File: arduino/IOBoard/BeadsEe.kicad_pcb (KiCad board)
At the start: 2 copper layers, 68.6 x 53.3 mm, 121 parts, among them J1 Servo Conn, J2 Servo Pow, J3 Supply Select, J4 I2C, P1 Power, P2 Analog, P3 Digital, P4 Digital, P5 CONN_01X01, P6 CONN_01X01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

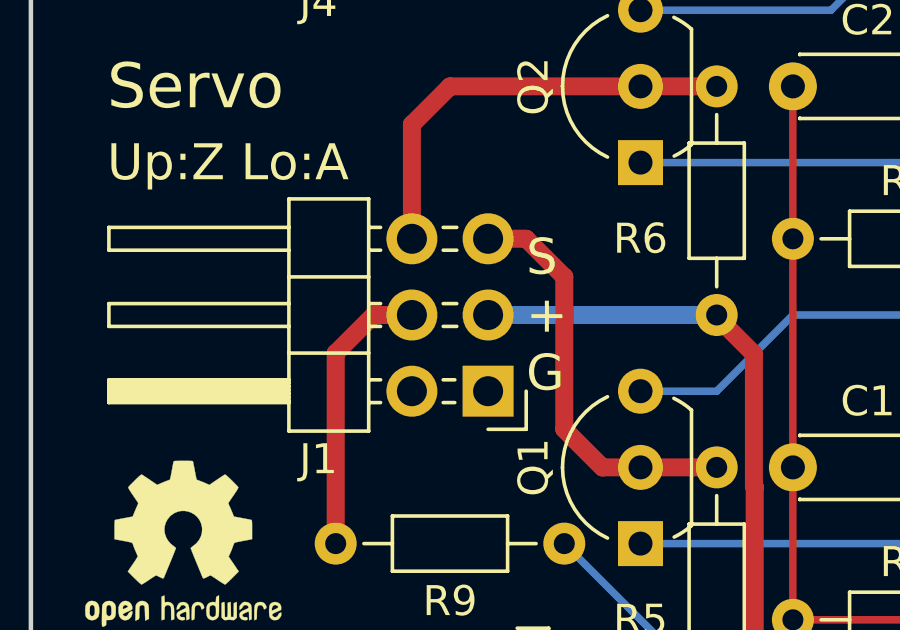
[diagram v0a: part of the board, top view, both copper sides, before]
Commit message: 配線を修正
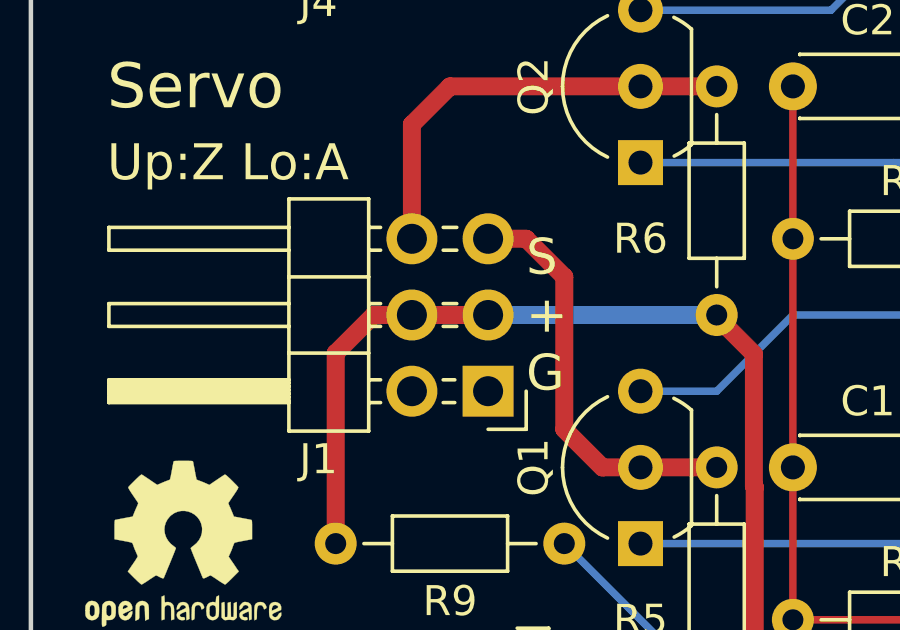
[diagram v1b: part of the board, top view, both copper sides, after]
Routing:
- net VS: track 40.2 -> 42.7 mm
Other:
- board text added: "Beads EE Control Board, Rev.1.0 2020.05 Setouchi ROS / myasu"
